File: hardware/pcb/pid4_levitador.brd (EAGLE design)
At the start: 180.3 x 137.2 mm, 128 parts, among them P1_C1 1u, P1_C2 1u, P1_J_IN VSENSOR, P1_J_OUT VPID, P1_J_PWR PWR, P1_POT1 22k, P1_POT2 220k, P1_POT3 22k, P1_R1 10k, P1_R10 1k, P1_R11 1M, P1_R12 160k, P1_R13 240k, P1_R14 96k, P1_R15 160k, P1_R2 10k, P1_R3 10k, P1_R4 10k, P1_R5 10k, P1_R6 1k, P1_R7 10k, P1_R8 10k, P1_R9 10k, P1_RBIAS 4.4k, P1_ROFFSET 10k, P1_U1 LM741, P1_U2 LM741, P1_U3 LM741, P1_U4 LM741, P1_U5 LM741, P1_U6 LM741, P1_U7 LM741, P2_C1 1u, P2_C2 1u, P2_J_IN VSENSOR, P2_J_OUT VPID, P2_J_PWR PWR, P2_POT1 22k, P2_POT2 220k, P2_POT3 22k, P2_R1 10k, P2_R10 1k, P2_R11 1M, P2_R12 160k, P2_R13 240k, P2_R14 96k, P2_R15 160k, P2_R2 10k, P2_R3 10k, P2_R4 10k, P2_R5 10k, P2_R6 1k, P2_R7 10k, P2_R8 10k, P2_R9 10k, P2_RBIAS 4.4k, P2_ROFFSET 10k, P2_U1 LM741, P2_U2 LM741, P2_U3 LM741, P2_U4 LM741, P2_U5 LM741, P2_U6 LM741, P2_U7 LM741, P3_C1 1u, P3_C2 1u, P3_J_IN VSENSOR, P3_J_OUT VPID, P3_J_PWR PWR, P3_POT1 22k, P3_POT2 220k, P3_POT3 22k, P3_R1 10k, P3_R10 1k, P3_R11 1M, P3_R12 160k, P3_R13 240k, P3_R14 96k, P3_R15 160k, P3_R2 10k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

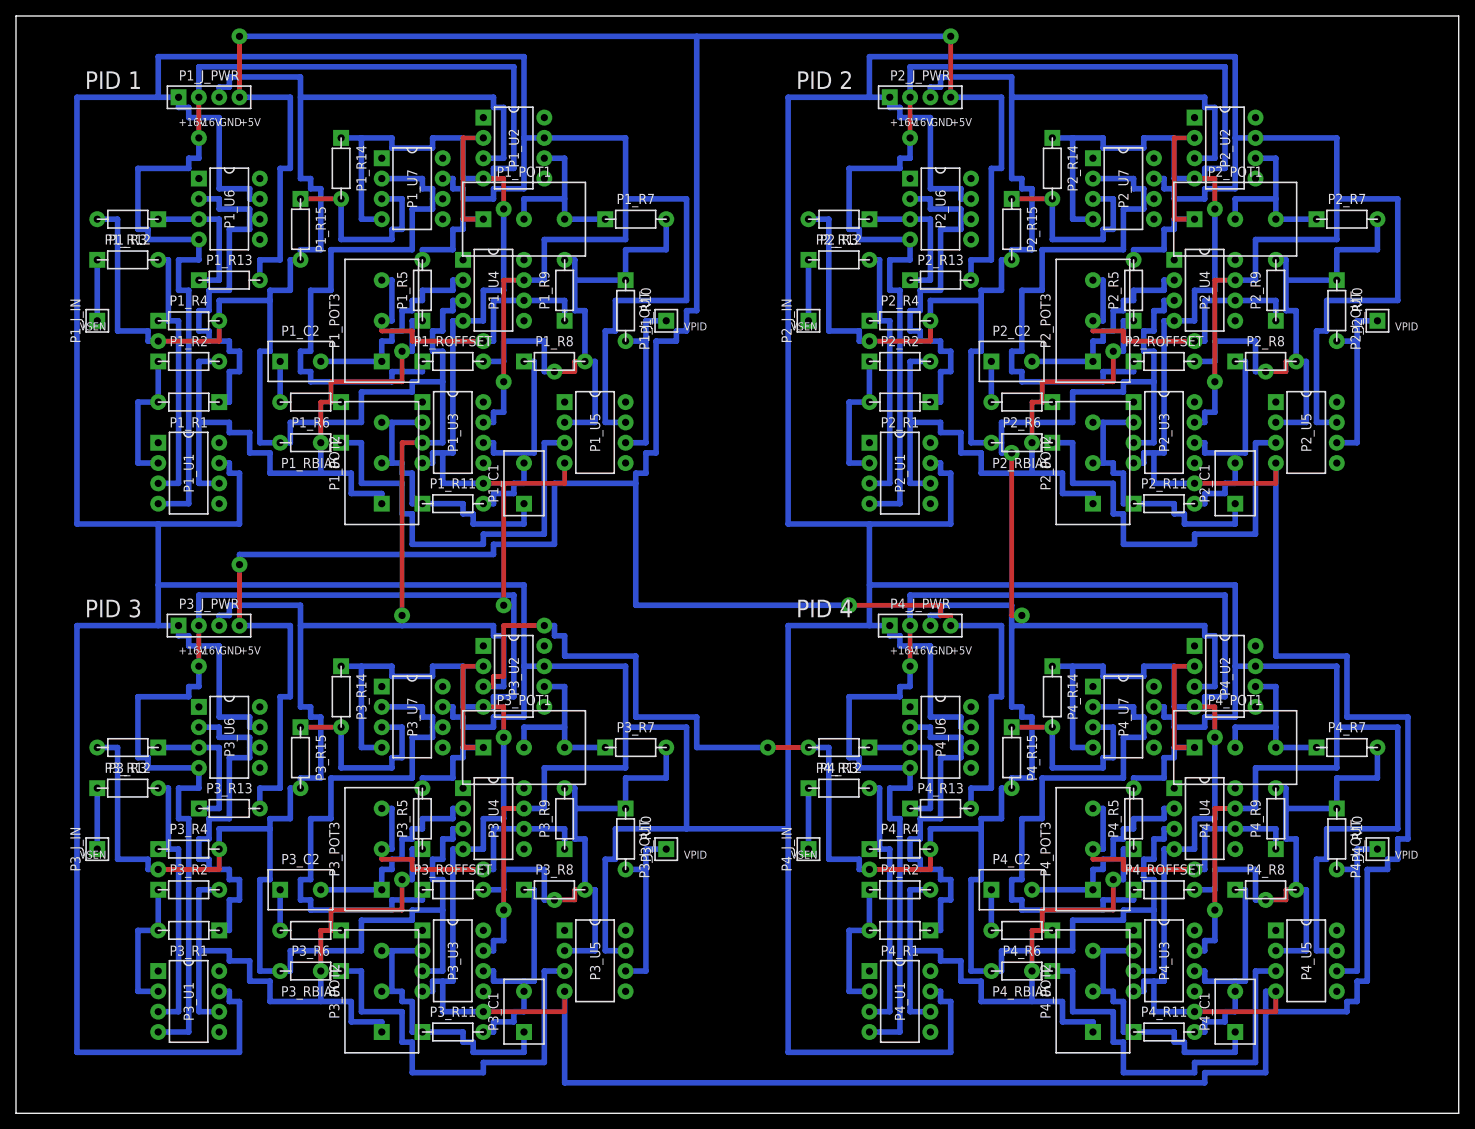
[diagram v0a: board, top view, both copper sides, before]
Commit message: Rehace la placa de 4 PID con TL074CN (2 por controlador, DIP-14) en lugar de LM741
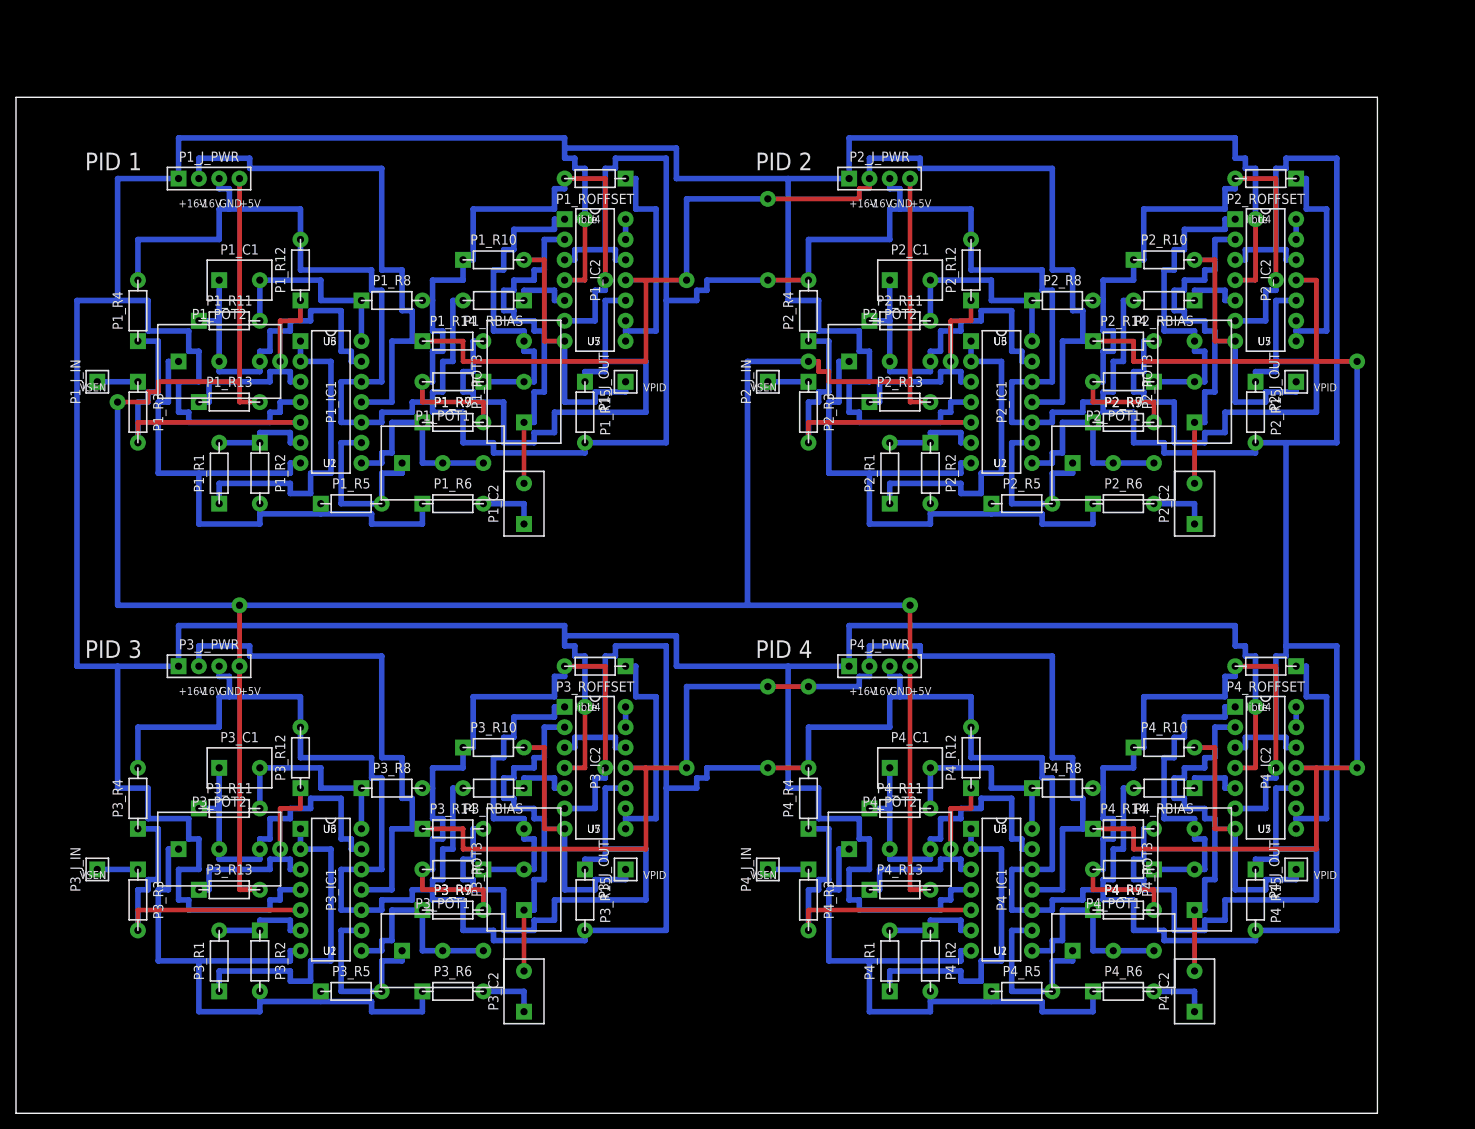
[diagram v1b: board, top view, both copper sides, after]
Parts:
- removed P1_U1, P1_U2, P1_U3, P1_U4, P1_U5, P1_U6, P1_U7, P2_U1, P2_U2, P2_U3, P2_U4, P2_U5, P2_U6, P2_U7, P3_U1, P3_U2, P3_U3, P3_U4, P3_U5, P3_U6, P3_U7, P4_U1, P4_U2, P4_U3, P4_U4, P4_U5, P4_U6, P4_U7: LM741, pid4:DIL08
- added P1_IC1, P1_IC2, P2_IC1, P2_IC2, P3_IC1, P3_IC2, P4_IC1, P4_IC2: TL074CN, pid4:DIL14
- moved P4_C1 54.4 mm to (109.2, 43.2), turned to 0 degrees
- moved P2_C1 51.4 mm to (109.2, 104.1), turned to 0 degrees
- moved P3_C1 50.4 mm to (25.4, 43.2), turned to 0 degrees
- moved P1_C1 47.2 mm to (25.4, 104.1), turned to 0 degrees
- moved P4_R11 43.3 mm to (106.7, 38.1)
- moved P1_R15 42.3 mm to (71.1, 91.4)
- moved P2_R11 40.2 mm to (106.7, 99.1)
- moved P3_R15 39.8 mm to (71.1, 30.5)
- moved P3_R11 39.5 mm to (22.9, 38.1)
- moved P2_R15 38.1 mm to (154.9, 91.4)
- moved P4_POT2 38.1 mm to (104.1, 33.0), turned to 0 degrees
- moved P3_ROFFSET 37.8 mm to (76.2, 55.9), turned to 180 degrees
- moved P2_R7 37.8 mm to (134.6, 86.4)
- moved P1_C2 36.6 mm to (63.5, 73.7), turned to 90 degrees
- moved P1_R11 36.1 mm to (22.9, 99.1)
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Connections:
- new net P1_SPARE: P1_IC2.13, P1_IC2.14
- new net P2_SPARE: P2_IC2.13, P2_IC2.14
- new net P3_SPARE: P3_IC2.13, P3_IC2.14
- new net P4_SPARE: P4_IC2.13, P4_IC2.14
- net +16V: now also P1_IC1.4, P1_IC2.4, P2_IC1.4, P2_IC2.4, P3_IC1.4, P3_IC2.4, P4_IC1.4, P4_IC2.4; no longer P1_U1.7, P1_U2.7, P1_U3.7, P1_U4.7, P1_U5.7, P1_U6.7, P1_U7.7, P2_U1.7, P2_U2.7, P2_U3.7, P2_U4.7, P2_U5.7, P2_U6.7, P2_U7.7, P3_U1.7, P3_U2.7, P3_U3.7, P3_U4.7, P3_U5.7, P3_U6.7, P3_U7.7, P4_U1.7, P4_U2.7, P4_U3.7, P4_U4.7, P4_U5.7, P4_U6.7, P4_U7.7
- net -16V: now also P1_IC1.11, P1_IC2.11, P2_IC1.11, P2_IC2.11, P3_IC1.11, P3_IC2.11, P4_IC1.11, P4_IC2.11; no longer P1_U1.4, P1_U2.4, P1_U3.4, P1_U4.4, P1_U5.4, P1_U6.4, P1_U7.4, P2_U1.4, P2_U2.4, P2_U3.4, P2_U4.4, P2_U5.4, P2_U6.4, P2_U7.4, P3_U1.4, P3_U2.4, P3_U3.4, P3_U4.4, P3_U5.4, P3_U6.4, P3_U7.4, P4_U1.4, P4_U2.4, P4_U3.4, P4_U4.4, P4_U5.4, P4_U6.4, P4_U7.4
- net GND: now also P1_IC1.10, P1_IC1.12, P1_IC2.12, P1_IC2.3, P2_IC1.10, P2_IC1.12, P2_IC2.12, P2_IC2.3, P3_IC1.10, P3_IC1.12, P3_IC2.12, P3_IC2.3, P4_IC1.10, P4_IC1.12, P4_IC2.12, P4_IC2.3; no longer P1_U2.3, P1_U3.3, P1_U4.3, P2_U2.3, P2_U3.3, P2_U4.3, P3_U2.3, P3_U3.3, P3_U4.3, P4_U2.3, P4_U3.3, P4_U4.3
- net P1_SUMN: now also P1_IC2.6; no longer P1_U5.2
- net P1_U1N: now also P1_IC1.6; no longer P1_U1.2
- net P1_U1P: now also P1_IC1.5; no longer P1_U1.3
- net P1_U2N: now also P1_IC1.9; no longer P1_U2.2
- net P1_U3N: now also P1_IC1.13; no longer P1_U3.2
- net P1_U4N: now also P1_IC2.2; no longer P1_U4.2
- net P1_U5P: now also P1_IC2.5; no longer P1_U5.3
- net P1_VD: now also P1_IC2.1; no longer P1_U4.6
- net P1_VE: now also P1_IC1.7; no longer P1_U1.6
- net P1_VI: now also P1_IC1.14; no longer P1_U3.6
- net P1_VOFF: now also P1_IC2.8, P1_IC2.9; no longer P1_U7.2, P1_U7.6
- net P1_VOFFD: now also P1_IC2.10; no longer P1_U7.3
- net P1_VP: now also P1_IC1.8; no longer P1_U2.6
- net P1_VPID: now also P1_IC2.7; no longer P1_U5.6
- net P1_VREF: now also P1_IC1.1, P1_IC1.2; no longer P1_U6.2, P1_U6.6
- net P1_VREFD: now also P1_IC1.3; no longer P1_U6.3
- net P2_SUMN: now also P2_IC2.6; no longer P2_U5.2
- net P2_U1N: now also P2_IC1.6; no longer P2_U1.2
- net P2_U1P: now also P2_IC1.5; no longer P2_U1.3
- net P2_U2N: now also P2_IC1.9; no longer P2_U2.2
- net P2_U3N: now also P2_IC1.13; no longer P2_U3.2
- net P2_U4N: now also P2_IC2.2; no longer P2_U4.2
- net P2_U5P: now also P2_IC2.5; no longer P2_U5.3
- net P2_VD: now also P2_IC2.1; no longer P2_U4.6
- net P2_VE: now also P2_IC1.7; no longer P2_U1.6
- net P2_VI: now also P2_IC1.14; no longer P2_U3.6
- net P2_VOFF: now also P2_IC2.8, P2_IC2.9; no longer P2_U7.2, P2_U7.6
- net P2_VOFFD: now also P2_IC2.10; no longer P2_U7.3
- net P2_VP: now also P2_IC1.8; no longer P2_U2.6
- net P2_VPID: now also P2_IC2.7; no longer P2_U5.6
- net P2_VREF: now also P2_IC1.1, P2_IC1.2; no longer P2_U6.2, P2_U6.6
- net P2_VREFD: now also P2_IC1.3; no longer P2_U6.3
- net P3_SUMN: now also P3_IC2.6; no longer P3_U5.2
- net P3_U1N: now also P3_IC1.6; no longer P3_U1.2
- net P3_U1P: now also P3_IC1.5; no longer P3_U1.3
- net P3_U2N: now also P3_IC1.9; no longer P3_U2.2
- net P3_U3N: now also P3_IC1.13; no longer P3_U3.2
- net P3_U4N: now also P3_IC2.2; no longer P3_U4.2
- net P3_U5P: now also P3_IC2.5; no longer P3_U5.3
- net P3_VD: now also P3_IC2.1; no longer P3_U4.6
- net P3_VE: now also P3_IC1.7; no longer P3_U1.6
- net P3_VI: now also P3_IC1.14; no longer P3_U3.6
- net P3_VOFF: now also P3_IC2.8, P3_IC2.9; no longer P3_U7.2, P3_U7.6
- net P3_VOFFD: now also P3_IC2.10; no longer P3_U7.3
- net P3_VP: now also P3_IC1.8; no longer P3_U2.6
- net P3_VPID: now also P3_IC2.7; no longer P3_U5.6
- net P3_VREF: now also P3_IC1.1, P3_IC1.2; no longer P3_U6.2, P3_U6.6
- net P3_VREFD: now also P3_IC1.3; no longer P3_U6.3
- net P4_SUMN: now also P4_IC2.6; no longer P4_U5.2
- net P4_U1N: now also P4_IC1.6; no longer P4_U1.2
- net P4_U1P: now also P4_IC1.5; no longer P4_U1.3
- net P4_U2N: now also P4_IC1.9; no longer P4_U2.2
- net P4_U3N: now also P4_IC1.13; no longer P4_U3.2
- net P4_U4N: now also P4_IC2.2; no longer P4_U4.2
- net P4_U5P: now also P4_IC2.5; no longer P4_U5.3
- net P4_VD: now also P4_IC2.1; no longer P4_U4.6
- net P4_VE: now also P4_IC1.7; no longer P4_U1.6
- net P4_VI: now also P4_IC1.14; no longer P4_U3.6
- net P4_VOFF: now also P4_IC2.8, P4_IC2.9; no longer P4_U7.2, P4_U7.6
- net P4_VOFFD: now also P4_IC2.10; no longer P4_U7.3
- net P4_VP: now also P4_IC1.8; no longer P4_U2.6
- net P4_VPID: now also P4_IC2.7; no longer P4_U5.6
- net P4_VREF: now also P4_IC1.1, P4_IC1.2; no longer P4_U6.2, P4_U6.6
- net P4_VREFD: now also P4_IC1.3; no longer P4_U6.3
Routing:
- net -16V: track 1201.4 -> 584.2 mm, vias 13 -> 7
- net +16V: track 1287.8 -> 698.5 mm
- net +5V: track 424.2 -> 332.7 mm
- net P3_U5P: track 53.3 -> 7.62 mm
- net P4_U5P: track 53.3 -> 7.62 mm
- net P1_U5P: track 53.3 -> 7.62 mm
- net P2_U5P: track 53.3 -> 7.62 mm
- net P4_VOFFD: track 25.4 -> 68.6 mm
- net P2_VOFFD: track 25.4 -> 68.6 mm
- net P1_VOFFD: track 25.4 -> 68.6 mm
- net P3_VOFFD: track 25.4 -> 68.6 mm
- net P2_VOFF: track 67.3 -> 29.2 mm
- net P4_VOFF: track 67.3 -> 29.2 mm
- net P3_VOFF: track 67.3 -> 29.2 mm
- net P1_VOFF: track 67.3 -> 29.2 mm
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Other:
- board size 180.3 x 137.2 mm -> 170.2 x 127 mm
- board text added: "U1"
- board text added: "U2"
- board text added: "U3"
- board text added: "U4"
- board text added: "U5"
- board text added: "U6"
- board text added: "U7"
- board text added: "libre"

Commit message: Agrega la etapa de potencia a cada uno de los 4 PID de la placa (TIP122, banco de sensado 10 x 1R, protección y bornes de bobina)
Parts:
- added P1_C3, P2_C3, P3_C3, P4_C3: 10n (opc.), pid4:CAP
- added P1_D1, P2_D1, P3_D1, P4_D1: 1N5408, pid4:DIODE
- added P1_D2, P2_D2, P3_D2, P4_D2: 1N4148, pid4:DIODE_S
- added P1_JP_GND, P2_JP_GND, P3_JP_GND, P4_JP_GND: GND-PGND, pid4:HDR2
- added P1_J_COIL, P2_J_COIL, P3_J_COIL, P4_J_COIL: BOBINA, pid4:TERM2
- added P1_J_VBOB, P2_J_VBOB, P3_J_VBOB, P4_J_VBOB: VBOB, pid4:TERM2
- added P1_POT4, P2_POT4, P3_POT4, P4_POT4: 10k, pid4:POT
- added P1_Q1, P2_Q1, P3_Q1, P4_Q1: TIP122, pid4:TO220
- added P1_R16, P1_RBASE, P2_R16, P2_RBASE, P3_R16, P3_RBASE, P4_R16, P4_RBASE: 270, pid4:RES
- added P1_R17, P2_R17, P3_R17, P4_R17: 56k, pid4:RES
- added P1_R18, P2_R18, P3_R18, P4_R18: 1k, pid4:RES
- added P1_RS, P2_RS, P3_RS, P4_RS: 10 x 1R 5W, pid4:RSBANK
- moved P1_C2 186.0 mm to (17.8, 254.0), turned to 270 degrees
- moved P2_C2 183.8 mm to (111.8, 254.0), turned to 270 degrees
- moved P1_R6 178.3 mm to (38.1, 254.0), turned to 180 degrees
- moved P2_R6 177.8 mm to (132.1, 254.0), turned to 180 degrees
- moved P2_R5 177.4 mm to (162.6, 248.9), turned to 270 degrees
- moved P1_R5 175.4 mm to (68.6, 248.9), turned to 270 degrees
- moved P2_R13 171.7 mm to (129.5, 259.1), turned to 90 degrees
- moved P2_POT2 171.2 mm to (165.1, 254.0), turned to 90 degrees
- moved P1_R13 170.7 mm to (35.6, 259.1), turned to 90 degrees
- moved P2_C1 169.6 mm to (157.5, 266.7), turned to 270 degrees
- moved P1_POT2 167.9 mm to (71.1, 254.0), turned to 90 degrees
- moved P1_POT3 167.6 mm to (22.9, 248.9), turned to 0 degrees
- moved P2_IC1 167.0 mm to (144.8, 261.6)
- moved P1_C1 167.0 mm to (63.5, 266.7), turned to 270 degrees
- moved P1_IC1 165.8 mm to (50.8, 261.6)
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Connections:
- removed net P1_SPARE: P1_IC2.13, P1_IC2.14
- removed net P2_SPARE: P2_IC2.13, P2_IC2.14
- removed net P3_SPARE: P3_IC2.13, P3_IC2.14
- removed net P4_SPARE: P4_IC2.13, P4_IC2.14
- new net P1_+VBOB: P1_D1.2, P1_J_COIL.1, P1_J_VBOB.1
- new net P1_BASE: P1_D2.2, P1_Q1.1
- new net P1_BASEA: P1_D2.1, P1_RBASE.2
- new net P1_COILN: P1_D1.1, P1_J_COIL.2, P1_Q1.2
- new net P1_INMU: P1_C3.1, P1_IC2.13, P1_R18.2
- new net P1_IOUT: P1_C3.2, P1_IC2.14, P1_RBASE.1
- new net P1_ISENSE: P1_Q1.3, P1_R18.1, P1_RS.10, P1_RS.11, P1_RS.12, P1_RS.13, P1_RS.14, P1_RS.15, P1_RS.6, P1_RS.7, P1_RS.8, P1_RS.9
- new net P1_PGND: P1_JP_GND.2, P1_J_VBOB.2, P1_RS.1, P1_RS.16, P1_RS.17, P1_RS.18, P1_RS.19, P1_RS.2, P1_RS.20, P1_RS.3, P1_RS.4, P1_RS.5
- new net P1_VCAL: P1_POT4.2, P1_R16.1
- new net P1_VDIV: P1_POT4.1, P1_R17.2
- new net P1_VINP: P1_IC2.12, P1_R16.2
- new net P2_+VBOB: P2_D1.2, P2_J_COIL.1, P2_J_VBOB.1
- new net P2_BASE: P2_D2.2, P2_Q1.1
- new net P2_BASEA: P2_D2.1, P2_RBASE.2
- new net P2_COILN: P2_D1.1, P2_J_COIL.2, P2_Q1.2
- new net P2_INMU: P2_C3.1, P2_IC2.13, P2_R18.2
- new net P2_IOUT: P2_C3.2, P2_IC2.14, P2_RBASE.1
- new net P2_ISENSE: P2_Q1.3, P2_R18.1, P2_RS.10, P2_RS.11, P2_RS.12, P2_RS.13, P2_RS.14, P2_RS.15, P2_RS.6, P2_RS.7, P2_RS.8, P2_RS.9
- new net P2_PGND: P2_JP_GND.2, P2_J_VBOB.2, P2_RS.1, P2_RS.16, P2_RS.17, P2_RS.18, P2_RS.19, P2_RS.2, P2_RS.20, P2_RS.3, P2_RS.4, P2_RS.5
- new net P2_VCAL: P2_POT4.2, P2_R16.1
- new net P2_VDIV: P2_POT4.1, P2_R17.2
- new net P2_VINP: P2_IC2.12, P2_R16.2
- new net P3_+VBOB: P3_D1.2, P3_J_COIL.1, P3_J_VBOB.1
- new net P3_BASE: P3_D2.2, P3_Q1.1
- new net P3_BASEA: P3_D2.1, P3_RBASE.2
- new net P3_COILN: P3_D1.1, P3_J_COIL.2, P3_Q1.2
- new net P3_INMU: P3_C3.1, P3_IC2.13, P3_R18.2
- new net P3_IOUT: P3_C3.2, P3_IC2.14, P3_RBASE.1
- new net P3_ISENSE: P3_Q1.3, P3_R18.1, P3_RS.10, P3_RS.11, P3_RS.12, P3_RS.13, P3_RS.14, P3_RS.15, P3_RS.6, P3_RS.7, P3_RS.8, P3_RS.9
- new net P3_PGND: P3_JP_GND.2, P3_J_VBOB.2, P3_RS.1, P3_RS.16, P3_RS.17, P3_RS.18, P3_RS.19, P3_RS.2, P3_RS.20, P3_RS.3, P3_RS.4, P3_RS.5
- new net P3_VCAL: P3_POT4.2, P3_R16.1
- new net P3_VDIV: P3_POT4.1, P3_R17.2
- new net P3_VINP: P3_IC2.12, P3_R16.2
- new net P4_+VBOB: P4_D1.2, P4_J_COIL.1, P4_J_VBOB.1
- new net P4_BASE: P4_D2.2, P4_Q1.1
- new net P4_BASEA: P4_D2.1, P4_RBASE.2
- new net P4_COILN: P4_D1.1, P4_J_COIL.2, P4_Q1.2
- new net P4_INMU: P4_C3.1, P4_IC2.13, P4_R18.2
- new net P4_IOUT: P4_C3.2, P4_IC2.14, P4_RBASE.1
- new net P4_ISENSE: P4_Q1.3, P4_R18.1, P4_RS.10, P4_RS.11, P4_RS.12, P4_RS.13, P4_RS.14, P4_RS.15, P4_RS.6, P4_RS.7, P4_RS.8, P4_RS.9
- new net P4_PGND: P4_JP_GND.2, P4_J_VBOB.2, P4_RS.1, P4_RS.16, P4_RS.17, P4_RS.18, P4_RS.19, P4_RS.2, P4_RS.20, P4_RS.3, P4_RS.4, P4_RS.5
- new net P4_VCAL: P4_POT4.2, P4_R16.1
- new net P4_VDIV: P4_POT4.1, P4_R17.2
- new net P4_VINP: P4_IC2.12, P4_R16.2
- net GND: now also P1_JP_GND.1, P1_POT4.3, P2_JP_GND.1, P2_POT4.3, P3_JP_GND.1, P3_POT4.3, P4_JP_GND.1, P4_POT4.3; no longer P1_IC2.12, P2_IC2.12, P3_IC2.12, P4_IC2.12
- net P1_VPID: now also P1_R17.1
- net P2_VPID: now also P2_R17.1
- net P3_VPID: now also P3_R17.1
- net P4_VPID: now also P4_R17.1
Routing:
- net -16V: track 584.2 -> 1014.7 mm, vias 7 -> 1
- net GND: track 899.2 -> 1188.7 mm, vias 2 -> 9
- net P2_PGND: track 0.00 -> 177.8 mm
- net P1_PGND: track 0.00 -> 177.8 mm
- net P4_PGND: track 0.00 -> 177.8 mm
- net P3_PGND: track 0.00 -> 177.8 mm
- net +5V: track 332.7 -> 431.8 mm
- net P4_INMU: track 0.00 -> 88.9 mm
- net P3_INMU: track 0.00 -> 88.9 mm
- net P2_INMU: track 0.00 -> 88.9 mm
- net P1_INMU: track 0.00 -> 88.9 mm
- net P3_VI: track 25.4 -> 106.7 mm
- net P2_VI: track 25.4 -> 106.7 mm
- net P1_VI: track 25.4 -> 106.7 mm
- net P4_VI: track 25.4 -> 106.7 mm
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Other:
- board size 170.2 x 127 mm -> 190.5 x 279.4 mm
- board text added: "+VBOB"
- board text added: "B"
- board text added: "BOB+"
- board text added: "BOB-"
- board text added: "C"
- board text added: "E"
- board text added: "PGND"
- board text added: "RS 10 x 1R/5W = 0.1R"
- board text added: "U8"
- board text removed: "libre"
